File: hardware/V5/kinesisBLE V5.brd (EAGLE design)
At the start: 122 x 86 mm, 24 parts, among them X1 JST-XH-02-PIN-ROUND-PAD, X2 JST-XH-02-PIN-ROUND-PAD

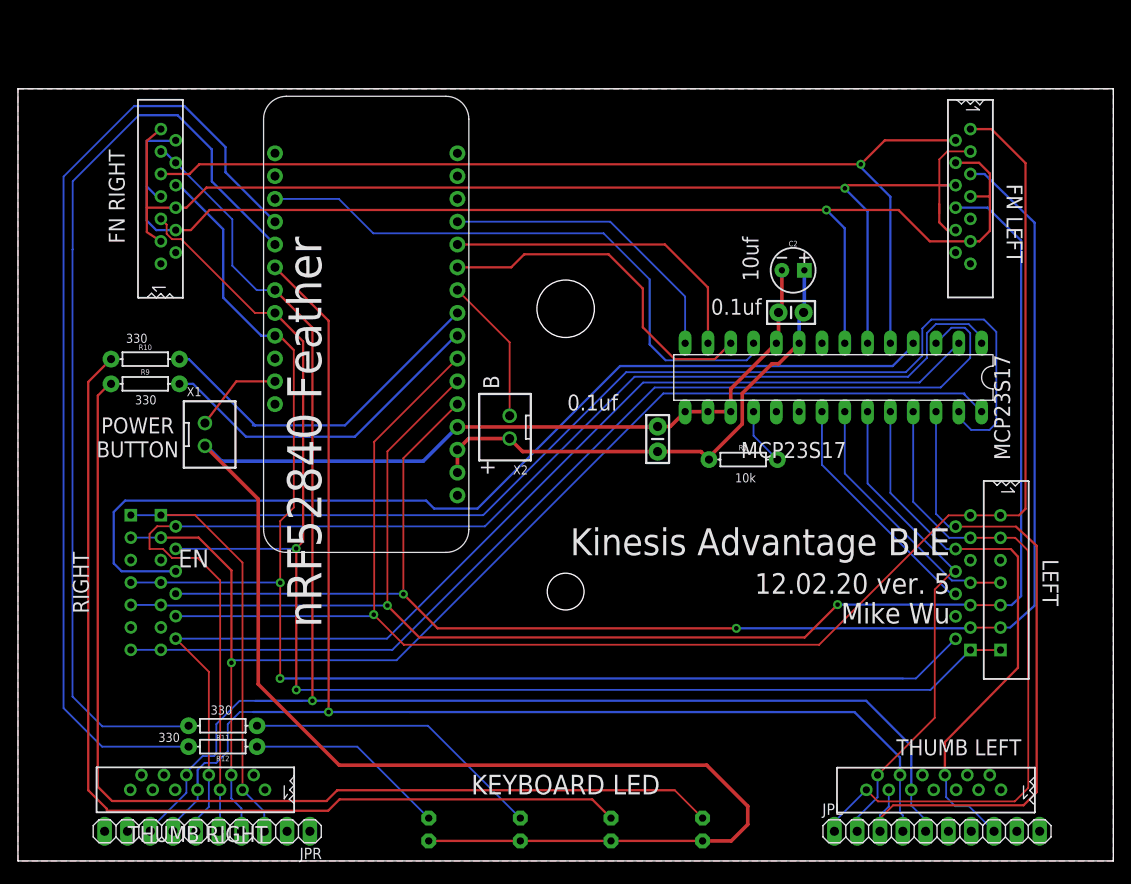
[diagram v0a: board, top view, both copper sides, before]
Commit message: increase / standardize trace widths
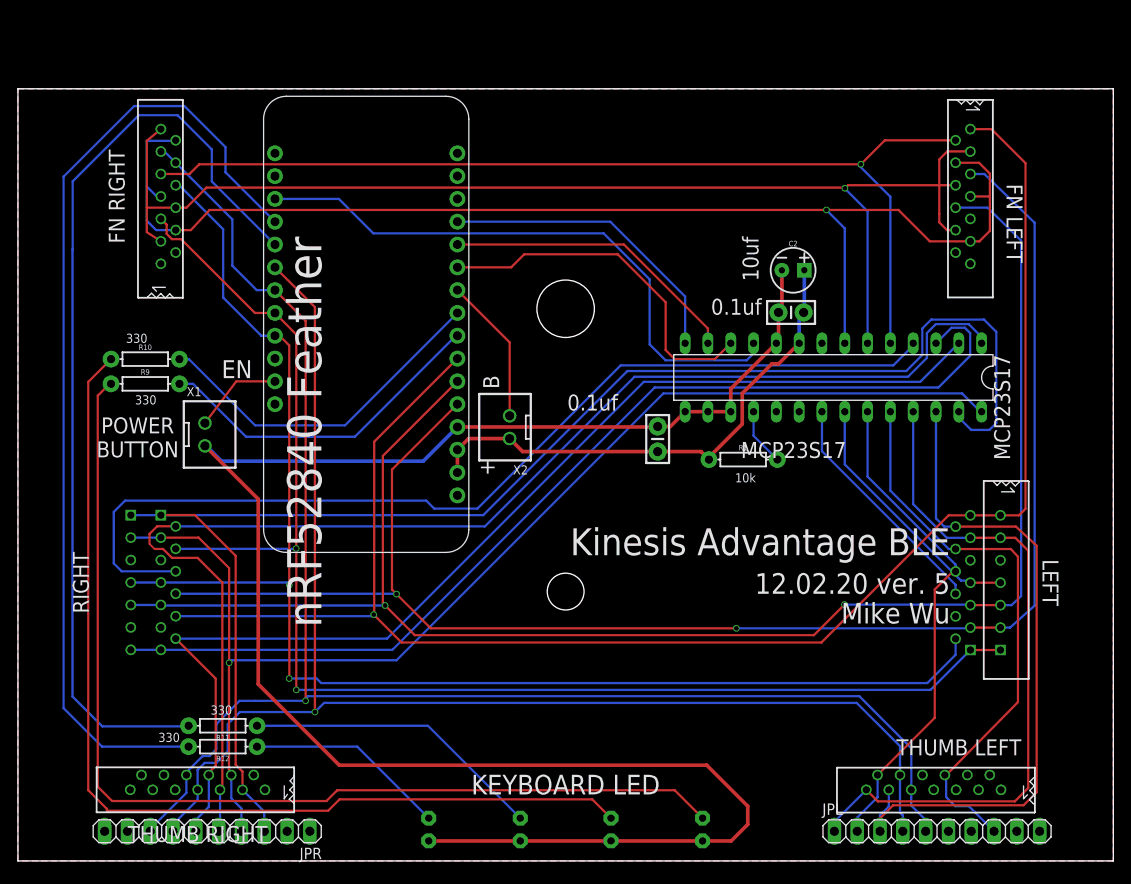
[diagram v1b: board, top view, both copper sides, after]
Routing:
- net MOSI: track 36.6 -> 33.4 mm
- net COL-N: track 139.5 -> 136.6 mm
- net ROW-7: track 153.1 -> 154.1 mm
- net ROW-6: track 176.6 -> 175.9 mm
- net ROW-3: track 173.9 -> 174.6 mm
- net COL-I: track 144.9 -> 144.2 mm
- net GND: track 207.8 -> 207.1 mm
- net ROW-4: track 156.2 -> 156.9 mm
- net COL-J: track 124.4 -> 125.1 mm
- net ROW-5: track 155.0 -> 154.3 mm
- net SCK: track 39.1 -> 39.7 mm
- net COL-B: track 29.3 -> 28.7 mm

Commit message: touches
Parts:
- added AMP: (no value), con-lstb:MA03-1
- added LS1: PS1240P02BT, PS1240P02BT:XDCR_PS1240P02BT
- added R2: 330, SparkFun-Resistors:AXIAL-0.3
- added R4: 1k, SparkFun-Resistors:AXIAL-0.3
- added U$8: KSC1815YTA, nspringkeeb:TO92-ECB
- moved C2 2.54 mm to (83.8, 65.8)
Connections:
- new net N$4: AMP.1, U$8.C
- new net N$5: AMP.2, LS1.1, R4.P$1
- new net N$7: R2.P$1, U$8.B
- new net SPK: AMP.3, R2.P$2, U$1.18
- net 3V@1: now also LS1.2, R4.P$2
- net GND: now also U$8.E
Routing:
- net SPK: track 0.00 -> 50.4 mm
- net N$5: track 0.00 -> 23.9 mm
- net 3V@1: track 58.0 -> 77.0 mm
- net N$7: track 0.00 -> 6.64 mm
- net N$4: track 0.00 -> 5.59 mm
- net GND: track 207.1 -> 211.0 mm
- net COL-M: track 111.5 -> 115.3 mm
- net ROW-3: track 174.6 -> 178.0 mm
- net KEY: track 108.7 -> 106.6 mm
- net SS: track 66.4 -> 64.5 mm
- net MISO: track 34.0 -> 32.4 mm
- net COL-J: track 125.1 -> 126.6 mm
- net COL-F: track 76.9 -> 75.5 mm
- net COL-E: track 77.0 -> 75.6 mm
- net ROW-6: track 175.9 -> 175.0 mm
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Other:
- board text added: "1k"
- board text added: "2-3 Amp Open Mute 1-2 Quiet"

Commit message: submit
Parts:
- moved R10 2.50 mm to (16.5, 56.9)
- moved R9 2.41 mm to (16.5, 53.9)
- moved JPL 1.85 mm to (100.6, 3.81)
- moved JPR 1.27 mm to (22.1, 4.06)
- moved C2 1.02 mm to (82.8, 65.8)
- moved U$8 1.02 mm to (75.9, 65.5)
- moved X1 0.72 mm to (21.3, 47.0)
- moved U$5 0.25 mm to (105.7, 31.0)
- moved R11 0.25 mm to (22.8, 15.3)
- moved U$4 0.25 mm to (16.3, 31.0)
- turned LED1 to 180 degrees
- turned LED2 to 180 degrees
- turned LED3 to 180 degrees
- turned LED4 to 180 degrees
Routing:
- net COL-L: track 110.7 -> 93.4 mm
- net SCR: track 105.6 -> 98.3 mm
- net KEY: track 106.6 -> 100.1 mm
- net ROW-3: track 178.0 -> 171.7 mm
- net GND: track 211.0 -> 204.7 mm
- net ROW-1: track 180.5 -> 177.1 mm
- net COL-M: track 115.3 -> 112.2 mm
- net CAPS: track 38.1 -> 35.7 mm
- net ROW-2: track 179.3 -> 177.4 mm
- net ROW-7: track 154.1 -> 152.3 mm
- net COL-J: track 126.6 -> 124.9 mm
- net COL-F: track 75.5 -> 77.1 mm
- net ROW-6: track 175.0 -> 173.3 mm
- net N$1: track 115.2 -> 113.6 mm
- net NUM: track 39.2 -> 37.8 mm
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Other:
- board size 122 x 86 mm -> 104.7 x 84.5 mm
- board text added: "21.09.20 ver. 5ns"
- board text added: "nspring"
- board text removed: "12.02.20 ver. 5"
- board text removed: "Mike Wu"
